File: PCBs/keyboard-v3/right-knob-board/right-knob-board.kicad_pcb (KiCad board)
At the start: 2 copper layers, 58 x 59 mm, 39 parts, among them J1 F31L-1A7H1-11008, M1 2206-100T, Q1 DMP21D0UFB-7B, Q2 DMN21D2UFB-7B, Q3 DMP21D0UFB-7B, SW1 SW_DIP_x01, SW2 SW_DIP_x01, SW3 SW_DIP_x01, U1 AS5600, U2 TMC6300-LA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

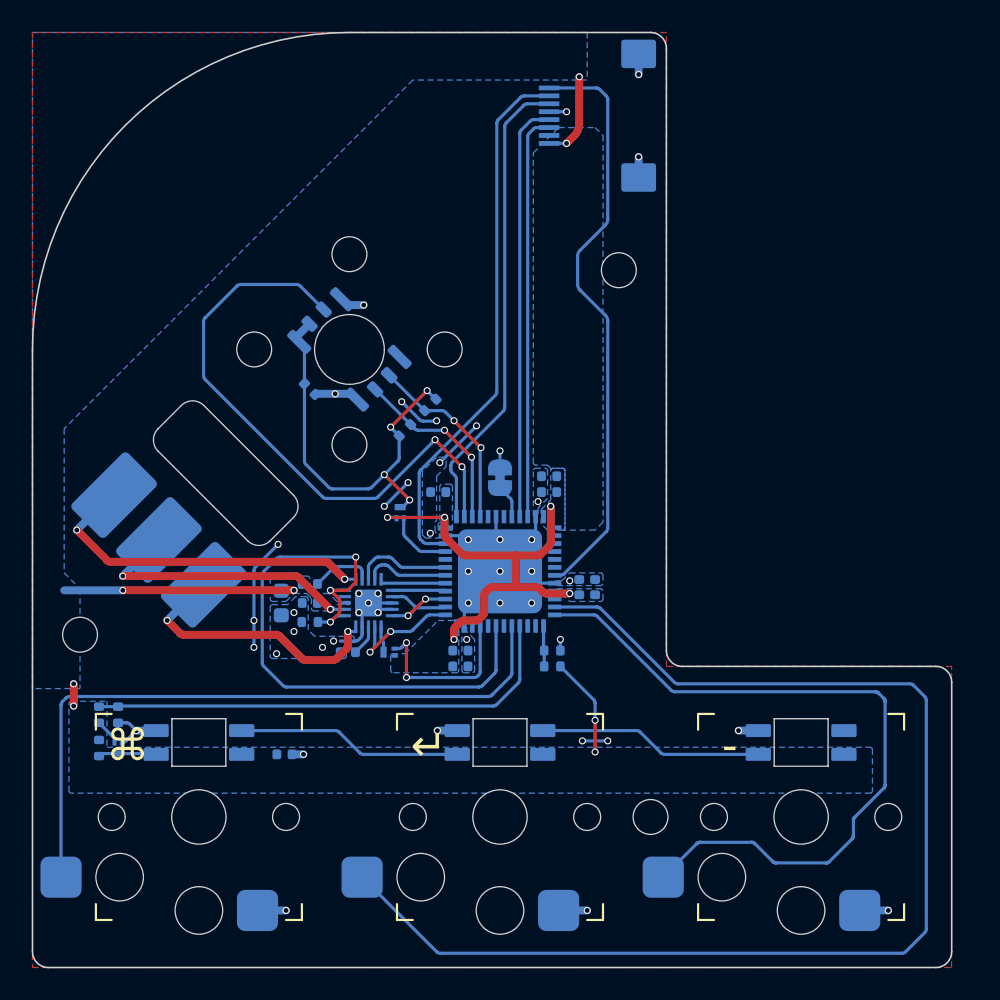
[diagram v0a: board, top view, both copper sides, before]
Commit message: Left knob board done
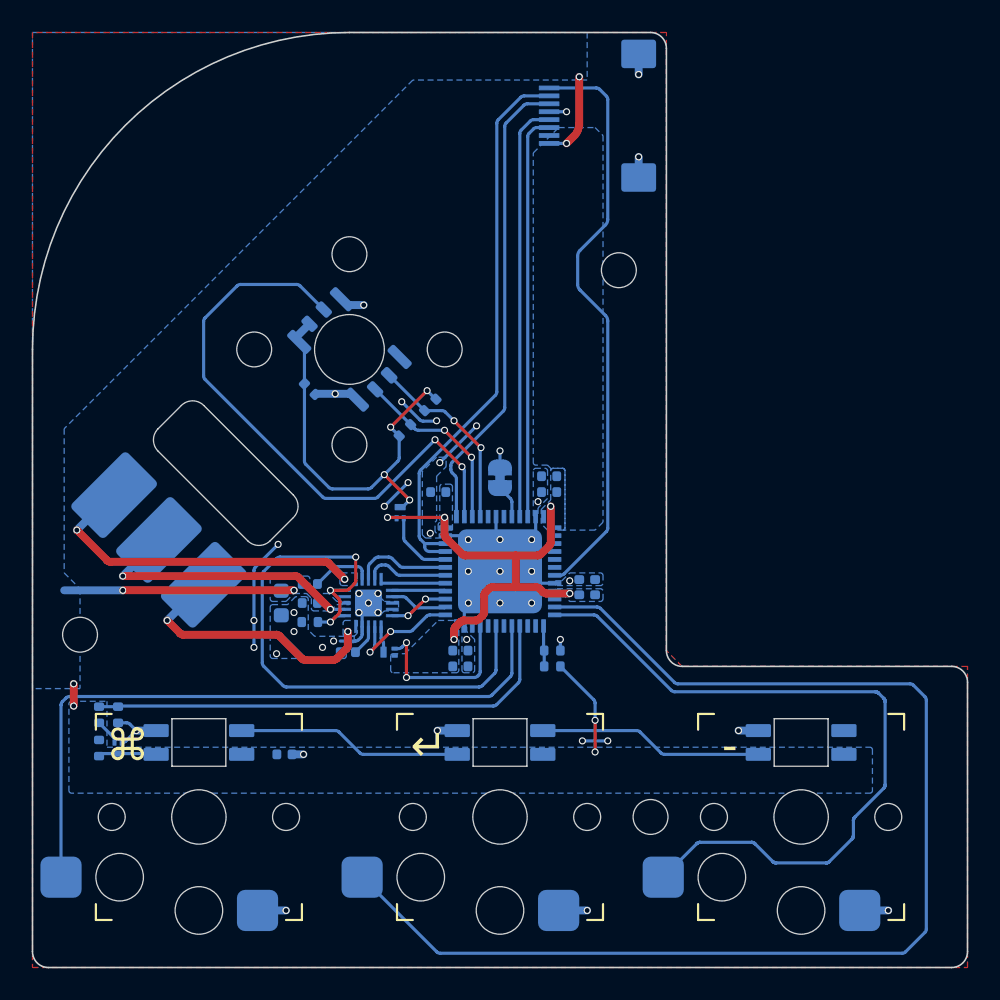
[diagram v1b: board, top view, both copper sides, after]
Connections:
- J1 pad 2: /SWDIO -> /SWDIO/~{INT}
- U3 pad 32: unconnected-(U3-PA11-Pad32) -> /~{ENC_EN}
- U3 pad 33: /~{ENC_EN} -> /SWDIO/~{INT}
- U3 pad 34: /SWDIO -> /SWDIO/~{INT}
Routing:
- net /SWDIO/~{INT}: track 0.00 -> 35.7 mm
- net /SWDIO: track 34.0 -> 0.00 mm
- net GND: track 66.3 -> 63.1 mm
- net /W: track 22.1 -> 21.4 mm
- net /U: track 17.4 -> 16.9 mm
- added copper zone on B.Cu, net /U
- added copper zone on B.Cu, net /W
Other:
- board size 58 x 59 mm -> 59 x 59 mm

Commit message: Keyboard v3 hardware done
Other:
- board text added: "Keyboard v3 Right Knob Board Ben Smith 2026"
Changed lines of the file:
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@@
 			(sketchdnponfab yes)
 			(crossoutdnponfab yes)
-			(subtractmaskfromsilk no)
+			(subtractmaskfromsilk yes)
 			(outputformat 1)
 			(mirror no)
@@
 	)
 	(gr_circle
+		(center 157 109.5)
+		(end 157 111.5)
+		(stroke
+			(width 0.1)
+			(type default)
+		)
+		(fill no)
+		(layer "F.SilkS")
+	)
+	(gr_circle
+		(center 157.069865 67.000971)
+		(end 157.269865 67.000971)
+		(stroke
+			(width 0)
+			(type solid)
+		)
+		(fill yes)
+		(layer "F.SilkS")
+	)
+	(gr_circle
+		(center 121 98)
+		(end 121 100)
+		(stroke
+			(width 0.1)
+			(type default)
+		)
+		(fill no)
+		(layer "F.SilkS")
+	)
+	(gr_circle
+		(center 155 75)
+		(end 155 77)
+		(stroke
+			(width 0.1)
+			(type default)
+		)
+		(fill no)
+		(layer "F.SilkS")
+	)
+	(gr_circle
+		(center 149.369865 67.000971)
+		(end 149.569865 67.000971)
+		(stroke
+			(width 0)
+			(type solid)
+		)
+		(fill yes)
+		(layer "B.SilkS")
+	)
+	(gr_circle
+		(center 138 86)
+		(end 138 84)
+		(stroke
+			(width 0.1)
+			(type default)
+		)
+		(fill no)
+		(layer "B.SilkS")
+	)
+	(gr_circle
+		(center 132 80)
+		(end 132 78)
+		(stroke
+			(width 0.1)
+			(type default)
+		)
+		(fill no)
+		(layer "B.SilkS")
+	)
+	(gr_circle
+		(center 144 80)
+		(end 144 78)
+		(stroke
+			(width 0.1)
+			(type default)
+		)
+		(fill no)
+		(layer "B.SilkS")
+	)
+	(gr_circle
+		(center 138 74)
+		(end 138 72)
+		(stroke
+			(width 0.1)
+			(type default)
+		)
+		(fill no)
+		(layer "B.SilkS")
+	)
+	(gr_circle
 		(center 138 80)
 		(end 157 80)
@@
 		)
 	)
+	(gr_text "Keyboard v3\nRight Knob Board\nBen Smith 2026"
+		(at 130 68.6 0)
+		(layer "B.SilkS")
+		(effects
+			(font
+				(size 1 1)
+				(thickness 0.1)
+			)
+			(justify mirror)
+		)
+	)
